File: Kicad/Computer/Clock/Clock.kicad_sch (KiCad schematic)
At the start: 7 parts, among them IC1 74VHC393FT, IC2 MC74VHC139DR2G, IC4 74VHC74M, IC5 DS1813R, IC6 MC74VHC04DR2G

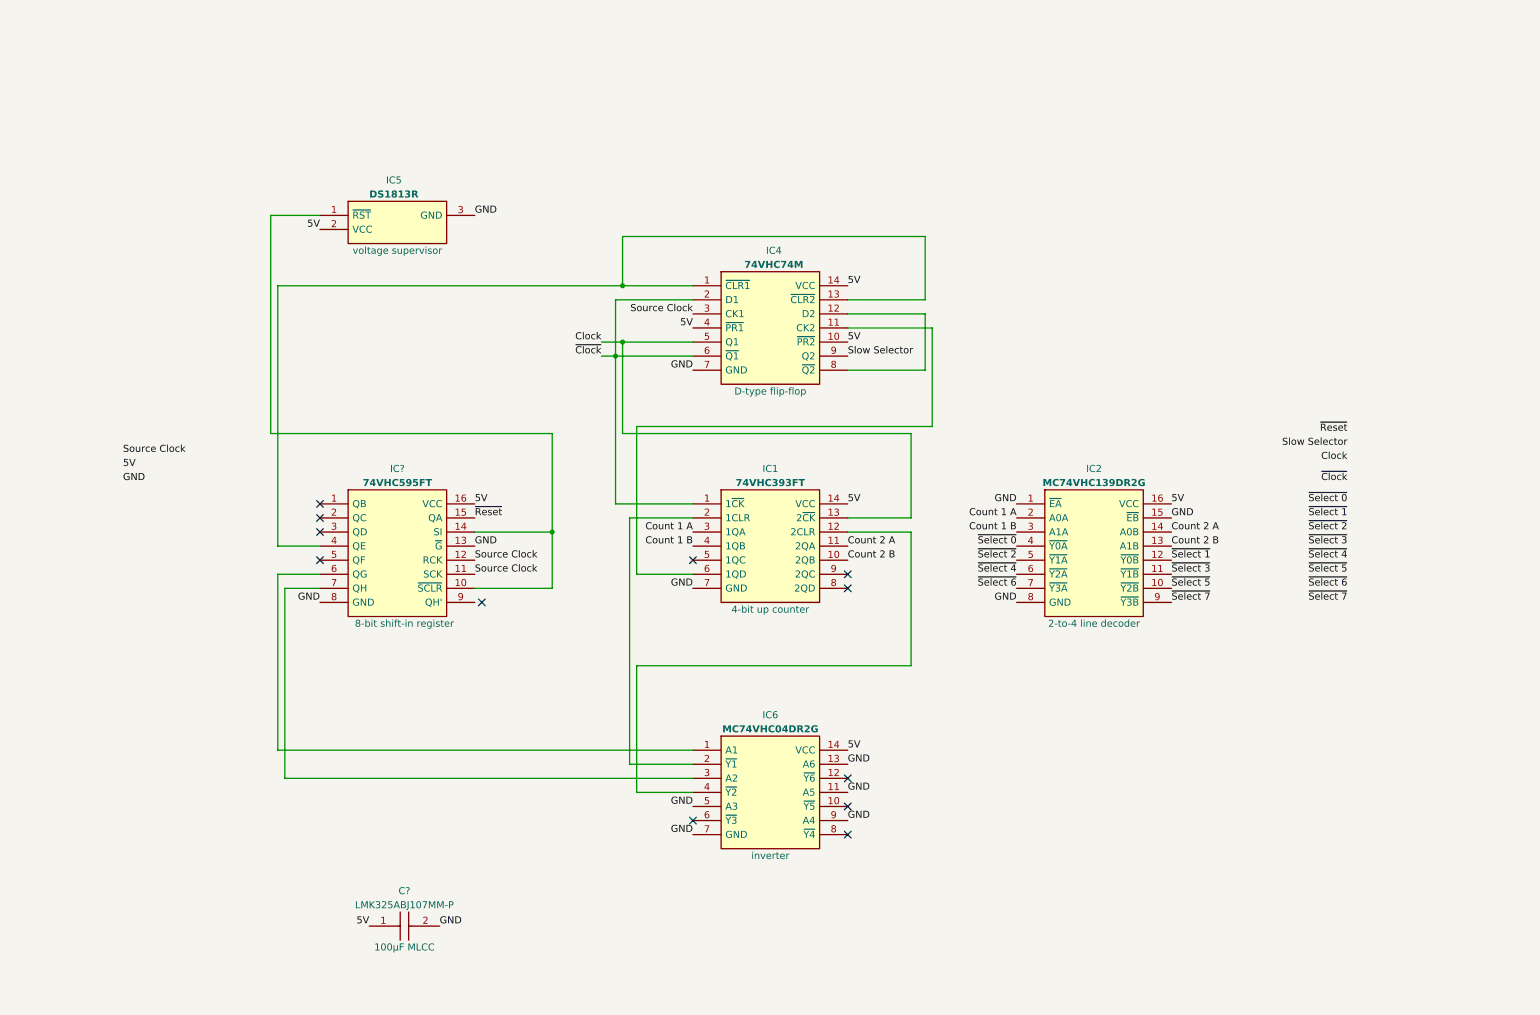
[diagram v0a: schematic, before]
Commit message: Completed clock schematic.
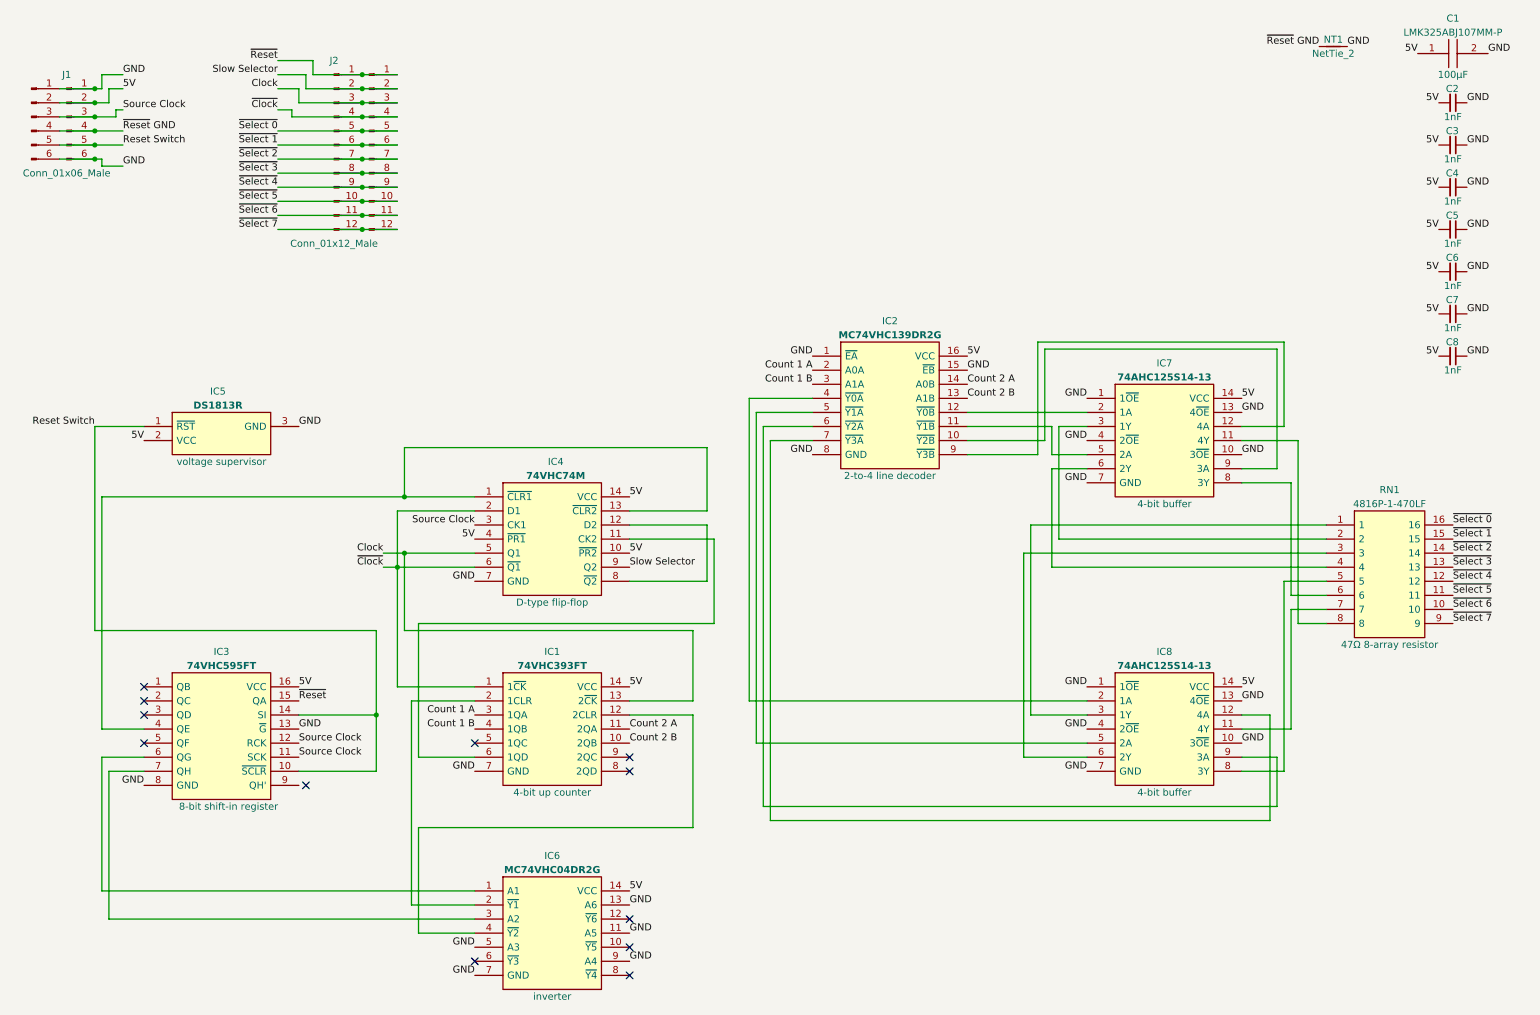
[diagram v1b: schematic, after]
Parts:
- added C2, C3, C4, C5, C6, C7, C8: C_Small, Capacitor_SMD:C_0805_2012Metric, symbol Device:C_Small
- added IC7, IC8: 74AHC125S14-13, SOIC127P600X173-14N, symbol Diodes_Inc:74AHC125S14-13
- added J1, J3: Conn_01x06_Male, Connector_PinHeader_2.54mm:PinHeader_1x06_P2.54mm_Vertical, symbol Connector:Conn_01x06_Male
- added J2, J4: Conn_01x12_Male, Connector_PinHeader_2.54mm:PinHeader_1x12_P2.54mm_Vertical, symbol Connector:Conn_01x12_Male
- added NT1: NetTie_2, NetTie:NetTie-2_SMD_Pad0.5mm, symbol Device:NetTie_2
- added RN1: 4816P-1-470LF, SOIC127P762X240-16N, symbol Bourns:4816P-1-470LF
- gave numbers to parts that had none: 2
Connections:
- net 5V: now also C2.2, C3.2, C4.2, C5.2, C6.2, C7.2, C8.2, IC7.14 (VCC), IC8.14 (VCC), J1.2 (Pin_2), J3.2 (Pin_2)
- net Clock: now also J2.3 (Pin_3), J4.3 (Pin_3)
- net GND: now also C2.1, C3.1, C4.1, C5.1, C6.1, C7.1, C8.1, IC7.1 (1~{OE}), IC7.10 (3~{OE}), IC7.13 (4~{OE}), IC7.4 (2~{OE}), IC7.7 (GND), IC8.1 (1~{OE}), IC8.10 (3~{OE}), IC8.13 (4~{OE}), IC8.4 (2~{OE}), IC8.7 (GND), J1.1 (Pin_1), J1.6 (Pin_6), J3.1 (Pin_1), J3.6 (Pin_6), NT1.2
- net Slow Selector: now also J2.2 (Pin_2), J4.2 (Pin_2)
- net Source Clock: now also J1.3 (Pin_3), J3.3 (Pin_3)
- net ~{Clock}: now also J2.4 (Pin_4), J4.4 (Pin_4)
- net ~{Reset}: now also J2.1 (Pin_1), J4.1 (Pin_1)
- net ~{Select 0}: now also J2.5 (Pin_5), J4.5 (Pin_5), RN1.16; no longer IC2.4 (~{Y0A})
- net ~{Select 1}: now also J2.6 (Pin_6), J4.6 (Pin_6), RN1.15; no longer IC2.12 (~{Y0B})
- net ~{Select 2}: now also J2.7 (Pin_7), J4.7 (Pin_7), RN1.14; no longer IC2.5 (~{Y1A})
- net ~{Select 3}: now also J2.8 (Pin_8), J4.8 (Pin_8), RN1.13; no longer IC2.11 (~{Y1B})
- net ~{Select 4}: now also J2.9 (Pin_9), J4.9 (Pin_9), RN1.12; no longer IC2.6 (~{Y2A})
- net ~{Select 5}: now also J2.10 (Pin_10), J4.10 (Pin_10), RN1.11; no longer IC2.10 (~{Y2B})
- net ~{Select 6}: now also J2.11 (Pin_11), J4.11 (Pin_11), RN1.10; no longer IC2.7 (~{Y3A})
- net ~{Select 7}: now also J2.12 (Pin_12), J4.12 (Pin_12), RN1.9; no longer IC2.9 (~{Y3B})
- net Reset Switch: now reaches IC3.10 (~{SCLR}), IC3.14 (SI), IC5.1 (~{RST})
- net Reset Switch: now also J1.5 (Pin_5), J3.5 (Pin_5)
- new net: IC8.11 (4Y), RN1.7
- new net: IC2.7 (~{Y3A}), IC8.12 (4A)
- new net: IC2.4 (~{Y0A}), IC8.2 (1A)
- new net: IC8.3 (1Y), RN1.1
- new net: IC2.5 (~{Y1A}), IC8.5 (2A)
- new net: IC8.6 (2Y), RN1.3
- new net: IC8.8 (3Y), RN1.5
- new net: IC2.6 (~{Y2A}), IC8.9 (3A)
- new net: IC7.11 (4Y), RN1.8
- new net: IC2.9 (~{Y3B}), IC7.12 (4A)
- new net: IC2.12 (~{Y0B}), IC7.2 (1A)
- new net: IC7.3 (1Y), RN1.2
- new net: IC2.11 (~{Y1B}), IC7.5 (2A)
- new net: IC7.6 (2Y), RN1.4
- new net: IC7.8 (3Y), RN1.6
- new net: IC2.10 (~{Y2B}), IC7.9 (3A)
- new net ~{Reset} GND: J1.4 (Pin_4), J3.4 (Pin_4), NT1.1
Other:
- moved on the sheet: C1, IC1, IC2, IC3, IC4, IC5, IC6

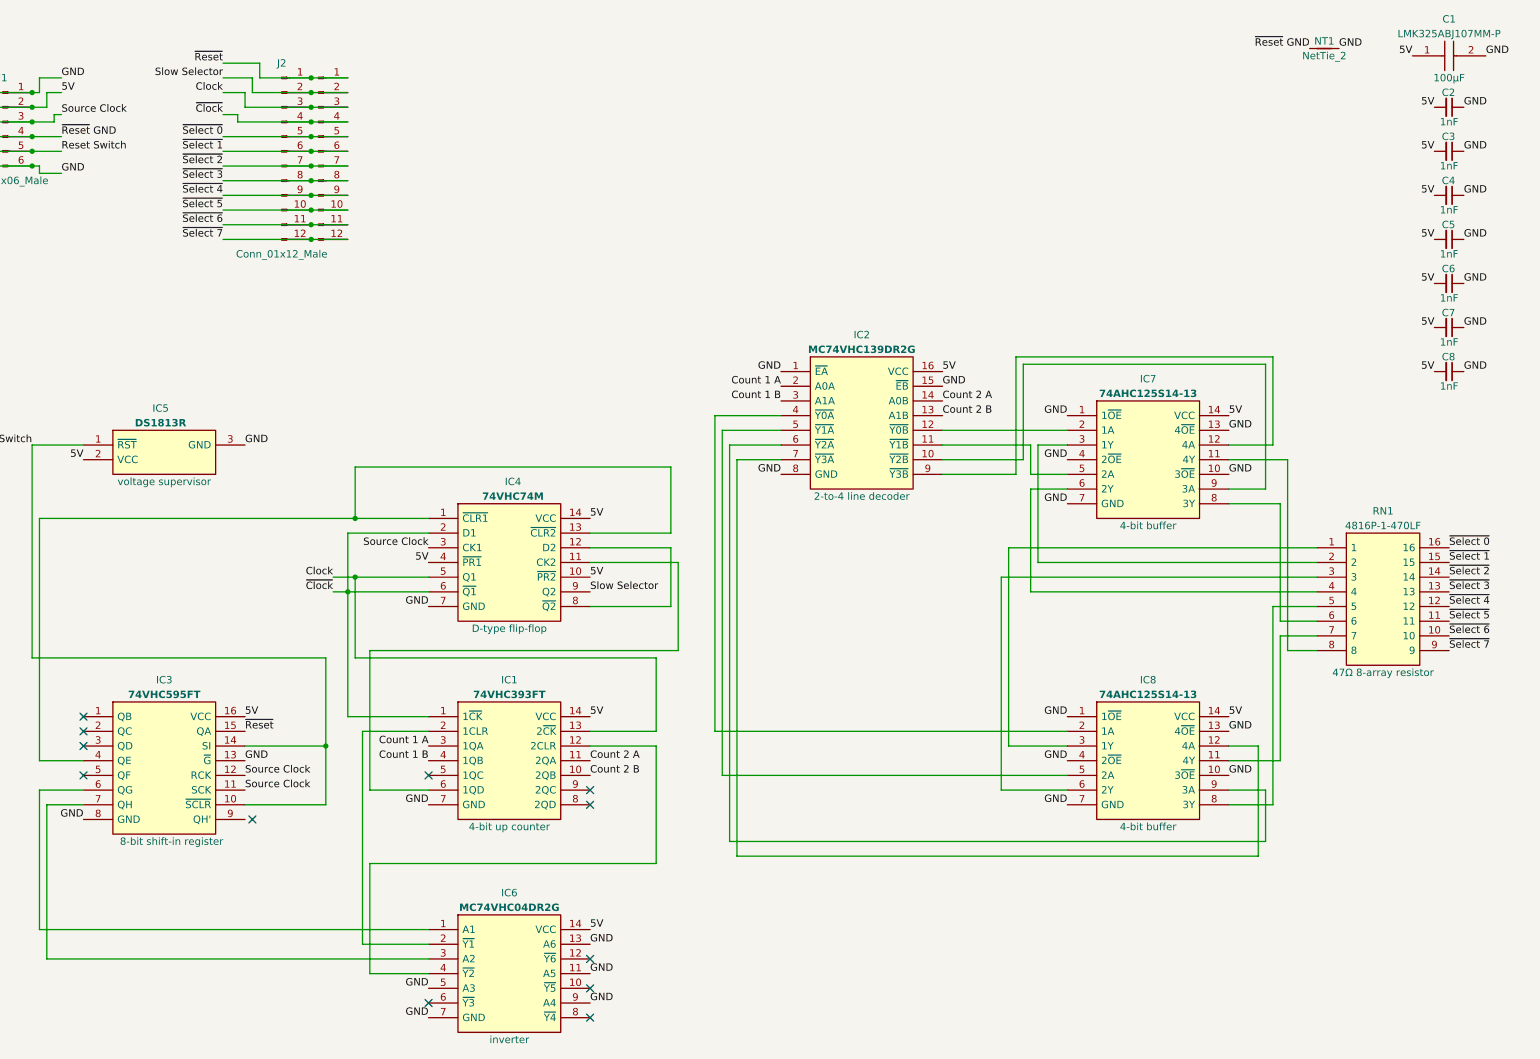
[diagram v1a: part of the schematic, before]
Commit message: Completed routing the Clock PCB.
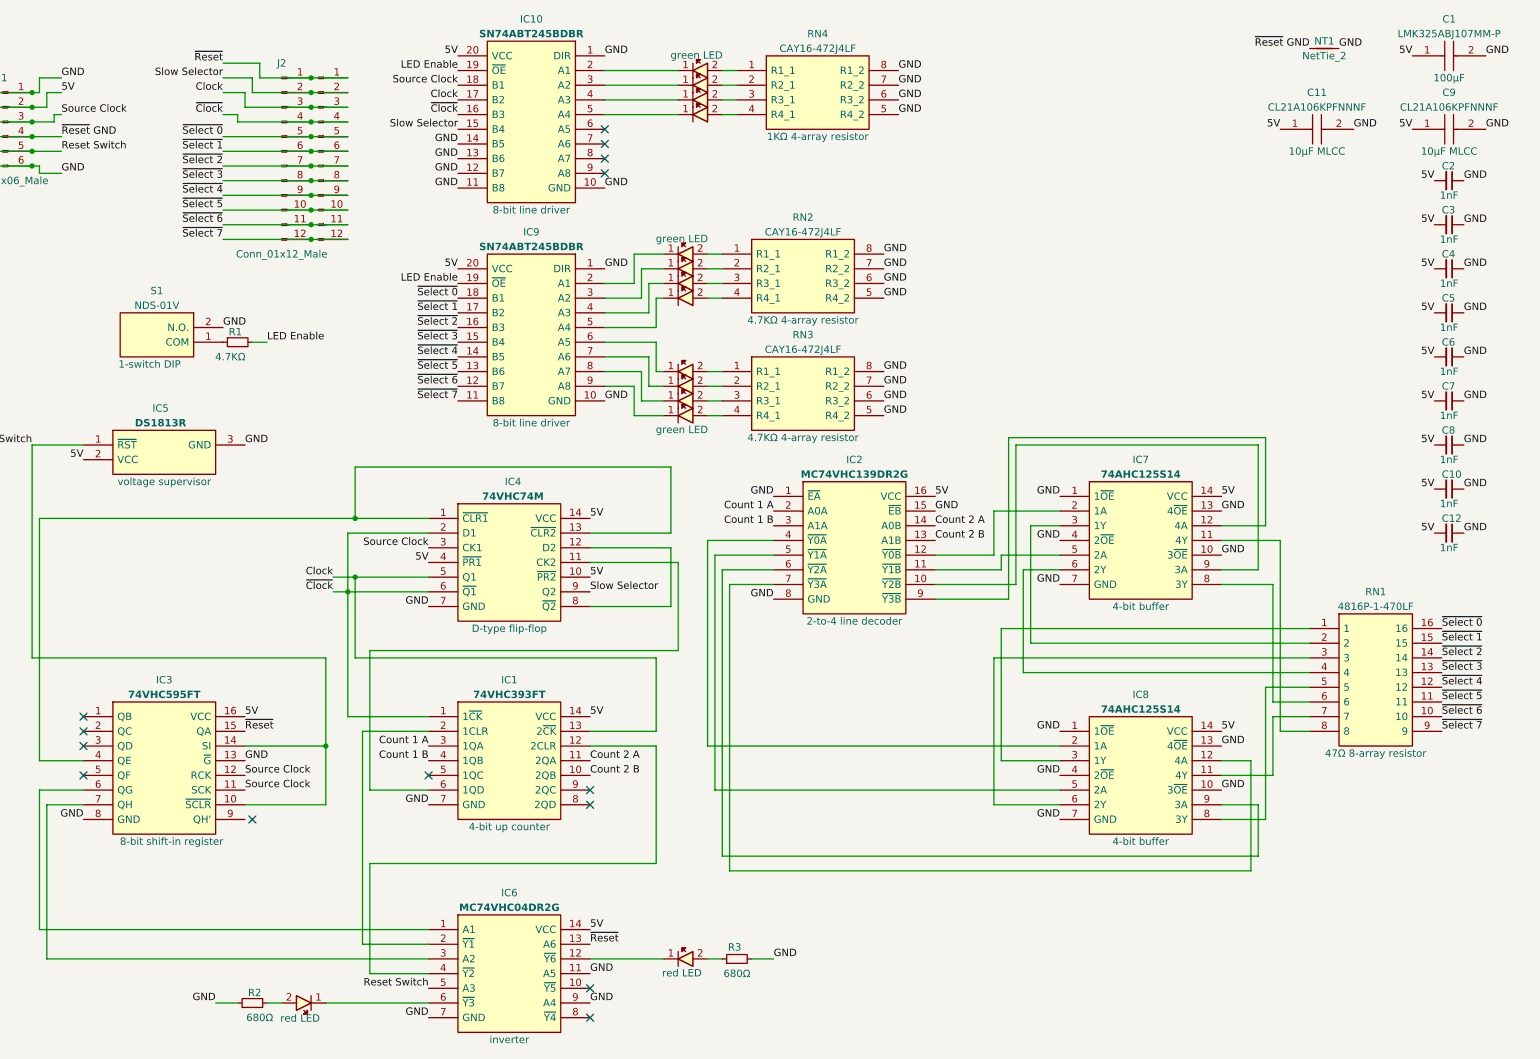
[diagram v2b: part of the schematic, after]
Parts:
- added C10, C12: C_Small, Capacitor_SMD:C_0805_2012Metric, symbol Device:C_Small
- added C11, C9: CL21A106KPFNNNF, CAPC2012X135N, symbol Samsung:CL21A106KPFNNNF
- added IC10, IC9: SN74ABT245BDBR, SOP65P780X200-20N, symbol Texas_Instruments:SN74ABT245BDBR
- added LED1, LED11, LED12, LED13, LED14, LED2, LED3, LED4, LED5, LED6, LED7, LED8: 150224VS73100A, 150224VS73100A, symbol Wurth_Elektronik:150224VS73100A
- added LED10, LED9: 150224SS73100, LEDM2314X131N, symbol Wurth_Elektronik:150224SS73100
- added R1, R2, R3: R_Small, Resistor_SMD:R_0805_2012Metric, symbol Device:R_Small
- added RN2, RN3, RN4: CAY16-472J4LF, CAY16472J4LF, symbol Bourns:CAY16-472J4LF
- added S1: NDS-01V, NDS01V, symbol Apem:NDS-01V
- IC7, IC8: value 74AHC125S14-13 -> 74AHC125S14
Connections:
- net 5V: now also C10.2, C11.1, C12.2, C9.1, IC10.20 (VCC), IC9.20 (VCC)
- net Clock: now also IC10.17 (B2)
- net GND: now also C10.1, C11.2, C12.1, C9.2, IC10.1 (DIR), IC10.10 (GND), IC10.11 (B8), IC10.12 (B7), IC10.13 (B6), IC10.14 (B5), IC9.1 (DIR), IC9.10 (GND), R2.2, R3.2, RN2.5 (R4_2), RN2.6 (R3_2), RN2.7 (R2_2), RN2.8 (R1_2), RN3.5 (R4_2), RN3.6 (R3_2), RN3.7 (R2_2), RN3.8 (R1_2), RN4.5 (R4_2), RN4.6 (R3_2), RN4.7 (R2_2), RN4.8 (R1_2), S1.2 (N.O.); no longer IC6.13 (A6), IC6.5 (A3)
- net Reset Switch: now also IC6.5 (A3)
- net Slow Selector: now also IC10.15 (B4)
- net Source Clock: now also IC10.18 (B1)
- net ~{Clock}: now also IC10.16 (B3)
- net ~{Reset}: now also IC6.13 (A6)
- net ~{Select 0}: now also IC9.18 (B1)
- net ~{Select 1}: now also IC9.17 (B2)
- net ~{Select 2}: now also IC9.16 (B3)
- net ~{Select 3}: now also IC9.15 (B4)
- net ~{Select 4}: now also IC9.14 (B5)
- net ~{Select 5}: now also IC9.13 (B6)
- net ~{Select 6}: now also IC9.12 (B7)
- net ~{Select 7}: now also IC9.11 (B8)
- net at IC6.12 (~{Y6}): now also LED10.1
- net at IC6.6 (~{Y3}): now also LED9.1
- new net: IC10.2 (A1), LED11.1
- new net: LED11.2, RN4.1 (R1_1)
- new net: IC9.2 (A1), LED1.1
- new net: IC9.3 (A2), LED2.1
- new net: IC9.4 (A3), LED3.1
- new net: IC9.5 (A4), LED4.1
- new net: IC9.6 (A5), LED5.1
- new net: IC9.7 (A6), LED6.1
- new net: IC9.8 (A7), LED7.1
- new net: IC9.9 (A8), LED8.1
- new net: LED8.2, RN3.4 (R4_1)
- new net: IC10.3 (A2), LED12.1
- new net: LED12.2, RN4.2 (R2_1)
- new net: IC10.4 (A3), LED13.1
- new net: IC10.5 (A4), LED14.1
- new net: LED5.2, RN3.1 (R1_1)
- new net: LED9.2, R2.1
- new net: R1.1, S1.1 (COM)
- new net: LED3.2, RN2.3 (R3_1)
- new net: LED14.2, RN4.4 (R4_1)
- new net: LED4.2, RN2.4 (R4_1)
- new net: LED10.2, R3.1
- new net: LED2.2, RN2.2 (R2_1)
- new net: LED13.2, RN4.3 (R3_1)
- new net: LED6.2, RN3.2 (R2_1)
- new net: LED7.2, RN3.3 (R3_1)
- new net: LED1.2, RN2.1 (R1_1)
- new net LED Enable: IC10.19 (~{OE}), IC9.19 (~{OE}), R1.2
- no-connect marks 12 -> 14
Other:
- moved on the sheet: C2, C3, C4, C5, C6, C7, C8, IC2, IC7, IC8, RN1

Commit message: Added a power LED.
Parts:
- added LED15: 150224SS73100, LEDM2314X131N, symbol Wurth_Elektronik:150224SS73100
- added R4, R5, R6, R7, R8: R_Small, Resistor_SMD:R_0805_2012Metric, symbol Device:R_Small
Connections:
- net 5V: now also LED15.2
- net Clock: now also R5.2; no longer IC1.13 (2~{CK}), IC4.5 (Q1)
- net GND: now also R8.2
- net Slow Selector: now also R7.2; no longer IC4.9 (Q2)
- net ~{Clock}: now also R6.2; no longer IC1.1 (1~{CK}), IC4.2 (D1), IC4.6 (~{Q1})
- net ~{Reset}: now also R4.2; no longer IC3.15 (QA)
- net at LED11.1: now also RN4.1 (R1_1); no longer IC10.2 (A1)
- net at LED11.2: now also IC10.2 (A1); no longer RN4.1 (R1_1)
- net at IC9.2 (A1): now also LED1.2; no longer LED1.1
- net at IC9.3 (A2): now also LED2.2; no longer LED2.1
- net at IC9.4 (A3): now also LED3.2; no longer LED3.1
- net at IC9.5 (A4): now also LED4.2; no longer LED4.1
- net at IC9.6 (A5): now also LED5.2; no longer LED5.1
- net at IC9.7 (A6): now also LED6.2; no longer LED6.1
- net at IC9.8 (A7): now also LED7.2; no longer LED7.1
- net at IC9.9 (A8): now also LED8.2; no longer LED8.1
- net at RN3.4 (R4_1): now also LED8.1; no longer LED8.2
- net at LED12.1: now also RN4.2 (R2_1); no longer IC10.3 (A2)
- net at LED12.2: now also IC10.3 (A2); no longer RN4.2 (R2_1)
- net at IC10.4 (A3): now also LED13.2; no longer LED13.1
- net at IC10.5 (A4): now also LED14.2; no longer LED14.1
- net at RN3.1 (R1_1): now also LED5.1; no longer LED5.2
- net Count 1 D: now reaches IC1.6 (1QD), IC4.11 (CK2)
- net at LED9.1: now also R2.1; no longer IC6.6 (~{Y3})
- net at LED9.2: now also IC6.6 (~{Y3}); no longer R2.1
- net at RN2.3 (R3_1): now also LED3.1; no longer LED3.2
- net at RN4.4 (R4_1): now also LED14.1; no longer LED14.2
- net at RN2.4 (R4_1): now also LED4.1; no longer LED4.2
- net at R3.1: now also LED10.1; no longer LED10.2
- net at RN2.2 (R2_1): now also LED2.1; no longer LED2.2
- net at IC6.12 (~{Y6}): now also LED10.2; no longer LED10.1
- net at RN4.3 (R3_1): now also LED13.1; no longer LED13.2
- net at RN3.2 (R2_1): now also LED6.1; no longer LED6.2
- net at RN3.3 (R3_1): now also LED7.1; no longer LED7.2
- net at RN2.1 (R1_1): now also LED1.1; no longer LED1.2
- new net: IC3.15 (QA), R4.1
- new net: IC1.1 (1~{CK}), IC4.2 (D1), IC4.6 (~{Q1}), R6.1
- new net: IC4.9 (Q2), R7.1
- new net: LED15.1, R8.1
- new net: IC1.13 (2~{CK}), IC4.5 (Q1), R5.1
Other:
- moved on the sheet: IC1, IC3, IC5, IC6, R1, R2, R3, S1
